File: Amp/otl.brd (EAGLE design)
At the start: 154.9 x 68.6 mm, 59 parts, among them X1 MOUNT-PAD2.0, X10 MOUNT-PAD2.0, X11 MOUNT-PAD2.0, X2 MOUNT-PAD2.0, X3 MOUNT-PAD2.0, X4 MOUNT-PAD2.0, X5 MOUNT-PAD2.0, X6 MOUNT-PAD2.0, X7 MOUNT-PAD2.0, X8 MOUNT-PAD2.0, X9 MOUNT-PAD2.0

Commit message: Made direct coupled
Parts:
- removed C13: 0.47uF, capacitor-wima:C22.5B11
- removed C14: 220uF/400V, my-cap:CPOL-RADIAL-25/12.5
- removed R25: 1.2k, my-res:AXIAL-0.8
- removed R26: 330, my-res:AXIAL-0.4
- removed R27: 1Meg, my-res:AXIAL-0.4
- removed R28: 100k, my-res:AXIAL-0.4
- added SJ1, SJ2: (no value), my-conn:SJ_2S-NO-LARGE
- added U1, U2: TLV431PTH, my-reg:TO-92
- C11: device capacitor-wima:C5B5.5 -> capacitor-wima:C22.5B11
- C12: value 1000uF/63V -> 220uF/400V; device my-cap:CPOL-RADIAL-16/7.5 -> my-cap:CPOL-RADIAL-25/12.5
- C2: value 0.47uF -> 470uF/63V; device capacitor-wima:C22.5B11 -> my-cap:CPOL-RADIAL-16/7.5
- C3: value 1000uF/63V -> 0.47uF; device my-cap:CPOL-RADIAL-16/7.5 -> capacitor-wima:C5B5.5
- C4: value 0.47uF -> 1000uF/63V; device capacitor-wima:C5B5.5 -> my-cap:CPOL-RADIAL-16/7.5
- C5: value 1000uF/63V -> 0.47uF; device my-cap:CPOL-RADIAL-16/7.5 -> capacitor-wima:C22.5B11
- C6: value 0.47uF -> 220uF/400V; device capacitor-wima:C22.5B11 -> my-cap:CPOL-RADIAL-25/12.5
- C7: value 220uF/400V -> 0.47uF; device my-cap:CPOL-RADIAL-25/12.5 -> capacitor-wima:C5B5.5
- C8: value 0.47uF -> 470uF/63V; device capacitor-wima:C5B5.5 -> my-cap:CPOL-RADIAL-16/7.5
- C9: device capacitor-wima:C22.5B11 -> capacitor-wima:C5B5.5
- R10, R22: value 750 -> 330; device my-res:AXIAL-0.8 -> my-res:AXIAL-0.4
- R11, R23: value 1.2k -> 1Meg; device my-res:AXIAL-0.8 -> my-res:AXIAL-0.4
- R12: value 330 -> 100k
- R14: value 100k -> 330
- R15: value 1Meg -> 68k; device my-res:AXIAL-0.4 -> my-res:AXIAL-0.8
- R16: value 330 -> 2k; device my-res:AXIAL-0.4 -> SparkFun-Electromechanical:3362U-2
- R17: value 240k -> 330
- R18: value 5.6k -> 750; device my-res:AXIAL-0.4 -> my-res:AXIAL-0.8
- R19: value 3Meg -> 1.5k; device my-res:AXIAL-0.4 -> my-res:AXIAL-0.8
- R20, R6: value 2.2Meg -> 750; device SparkFun-Electromechanical:3362U-2 -> my-res:AXIAL-0.8
- R21, R7: value 330 -> 1.5k; device my-res:AXIAL-0.4 -> my-res:AXIAL-0.8
- R24: value 750 -> 100k; device my-res:AXIAL-0.8 -> my-res:AXIAL-0.4
- R3: value 240k -> 68k; device my-res:AXIAL-0.4 -> my-res:AXIAL-0.8
- R4: value 5.6k -> 2k; device my-res:AXIAL-0.4 -> SparkFun-Electromechanical:3362U-2
- R5: value 3Meg -> 330
- R9: value 1.2k -> 1.5k
- moved X9 130.8 mm to (20.3, 34.3)
- moved X7 123.4 mm to (26.7, 22.9)
- moved R14 106.7 mm to (119.4, 47.0), turned to 0 degrees
- moved X3 105.6 mm to (132.1, 52.1)
- moved X11 102.9 mm to (26.7, 40.6)
- moved C7 101.2 mm to (109.2, 49.5), turned to 90 degrees
- moved X5 91.1 mm to (110.5, 63.5)
- moved X6 91.1 mm to (110.5, 5.08)
- moved C10 86.4 mm to (39.4, 43.2)
- moved R24 84.8 mm to (14.0, 38.1), turned to 180 degrees
- moved R19 74.9 mm to (39.4, 62.2), turned to 0 degrees
- moved C3 73.7 mm to (52.1, 22.9), turned to 0 degrees
- moved R13 59.4 mm to (119.4, 52.1), turned to 0 degrees
- moved C6 58.0 mm to (14.0, 15.2), turned to 0 degrees
- moved R17 53.9 mm to (74.9, 52.1)
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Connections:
- removed net N$22: C9.2, R20.2, R21.P$1
- removed net N$7: R5.P$1, R6.3
- net GND: now also C2.2, C7.2, C9.2, R12.P$1, R16.1, R19.P$1, R21.P$1, R24.P$1, R4.1, R7.P$1, SJ1.1, SJ2.1, U1.2, U2.2, X10.P$1, X11.P$1, X7.P$1, X8.P$1, X9.P$1; no longer C11.2, C12.2, C5.2, R14.P$1, R15.P$1, R18.P$1, R20.1, R25.P$1, R27.P$1, R28.P$1, R4.P$1, R6.1, X2.P$1, X3.P$1, X4.P$1, X5.P$1, X6.P$1
- net HT_L: now also R6.P$2, X6.P$1; no longer R10.P$2, R5.P$2, X11.P$1
- net HT_R: now also R15.P$2, R18.P$2, R20.P$2, X5.P$1; no longer R17.P$2, R19.P$2, R22.P$2, R24.P$2, X1.P$1
- net IN_L: now also X1.P$1; no longer X7.P$1
- net IN_R: now also R13.P$2, R14.P$1, X3.P$1; no longer R15.P$2, R16.P$1, X9.P$1
- net N$1: now also C5.1, R6.P$1; no longer C6.1, R10.P$1
- net N$10: now also R22.P$1; no longer R26.P$1
- net N$11: now also C6.1; no longer C7.1
- net N$12: now also C10.1, C9.1, R19.P$2, R21.P$2; no longer C11.1, C12.1, R23.P$2, R25.P$2
- net N$13: now also C11.2, R22.P$2, R23.P$2; no longer C13.2, R26.P$2, R27.P$2
- net N$14: now also R17.P$2; no longer R21.P$2
- net N$15: now also R16.2, SJ2.2, U2.1; no longer R19.P$1, R20.3
- net N$16: now also C7.1, R16.3, U2.3; no longer C10.1, R18.P$2
- net N$17: now also R15.P$1; no longer C9.1
- net N$18: now also C12.1; no longer C14.1
- net N$2: now also C11.1, R18.P$1, R20.P$1; no longer C13.1, R22.P$1, R24.P$1
- net N$20: now also R4.2, SJ1.2, U1.1; no longer C2.2, R6.2, R7.P$1
- net N$21: now also R14.P$2; no longer R16.P$2
- net N$3: now also R10.P$1; no longer R12.P$1
- net N$4: now also C2.1, R4.3, U1.3; no longer C3.1, R4.P$2
- net N$5: now also C3.1, R7.P$2; no longer C5.1, R11.P$2
- net N$6: now also C5.2, R10.P$2, R11.P$2; no longer C6.2, R12.P$2, R13.P$2
- net N$8: now also R5.P$2; no longer R7.P$2
- net N$9: now also R5.P$1; no longer C2.1
- net OUT_L: now also C6.2, R12.P$2, X2.P$1; no longer C7.2, R14.P$2, X8.P$1
- net OUT_R: now also C12.2, R24.P$2, X4.P$1; no longer C14.2, R28.P$2, X10.P$1
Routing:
- net N$22: track 44.7 -> 0.00 mm
- net N$4: track 39.8 -> 73.3 mm, vias 0 -> 3
- net N$20: track 44.7 -> 16.6 mm
- net N$16: track 36.8 -> 62.6 mm, vias 0 -> 3
- net N$21: track 21.2 -> 13.3 mm
- net N$15: track 7.71 -> 15.5 mm
- net N$7: track 7.73 -> 0.00 mm
- net N$17: track 61.8 -> 56.3 mm
- net N$19: track 11.0 -> 7.62 mm
- net N$9: track 58.9 -> 56.3 mm
- net HT_L: track 31.4 -> 29.3 mm
- net HT_R: track 31.4 -> 29.3 mm
- net IN_R: track 18.1 -> 19.9 mm
- net IN_L: track 18.1 -> 19.9 mm
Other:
- board size 154.9 x 68.6 mm -> 137.2 x 68.6 mm
- board text added: "GND"
- board text removed: "Vp"
- board text removed: "Vp/2"

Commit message: Tubes' names added
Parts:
- V1: value (none) -> 6SN7-GTB
- V2, V3: value (none) -> 6AS7-G
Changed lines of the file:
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@@
 <attribute name="VALUE" x="33.401" y="12.319" size="0.8128" layer="27" font="vector" ratio="20"/>
 </element>
-<element name="V1" library="my-tubes" package="OKTAL-OUTLET" value="" x="132.08" y="34.29" smashed="yes" rot="R90">
+<element name="V1" library="my-tubes" package="OKTAL-OUTLET" value="6SN7-GTB" x="132.08" y="34.29" smashed="yes" rot="R90">
 <attribute name="NAME" x="129.54" y="33.655" size="0.8128" layer="25" font="vector" ratio="20" rot="R90"/>
 <attribute name="VALUE" x="138.43" y="31.75" size="0.8128" layer="27" font="vector" ratio="15" rot="R90"/>
 </element>
-<element name="V2" library="my-tubes" package="OKTAL-OUTLET" value="" x="67.31" y="5.08" smashed="yes" rot="R180">
+<element name="V2" library="my-tubes" package="OKTAL-OUTLET" value="6AS7-G" x="67.31" y="5.08" smashed="yes" rot="R180">
 <attribute name="NAME" x="67.945" y="2.54" size="0.8128" layer="25" font="vector" ratio="20" rot="R180"/>
 <attribute name="VALUE" x="69.85" y="11.43" size="0.8128" layer="27" font="vector" ratio="15" rot="R180"/>
 </element>
-<element name="V3" library="my-tubes" package="OKTAL-OUTLET" value="" x="67.31" y="63.5" smashed="yes" rot="R180">
+<element name="V3" library="my-tubes" package="OKTAL-OUTLET" value="6AS7-G" x="67.31" y="63.5" smashed="yes" rot="R180">
 <attribute name="NAME" x="67.945" y="67.31" size="0.8128" layer="25" font="vector" ratio="20" rot="R180"/>
 <attribute name="VALUE" x="69.85" y="69.85" size="0.8128" layer="27" font="vector" ratio="15" rot="R180"/>

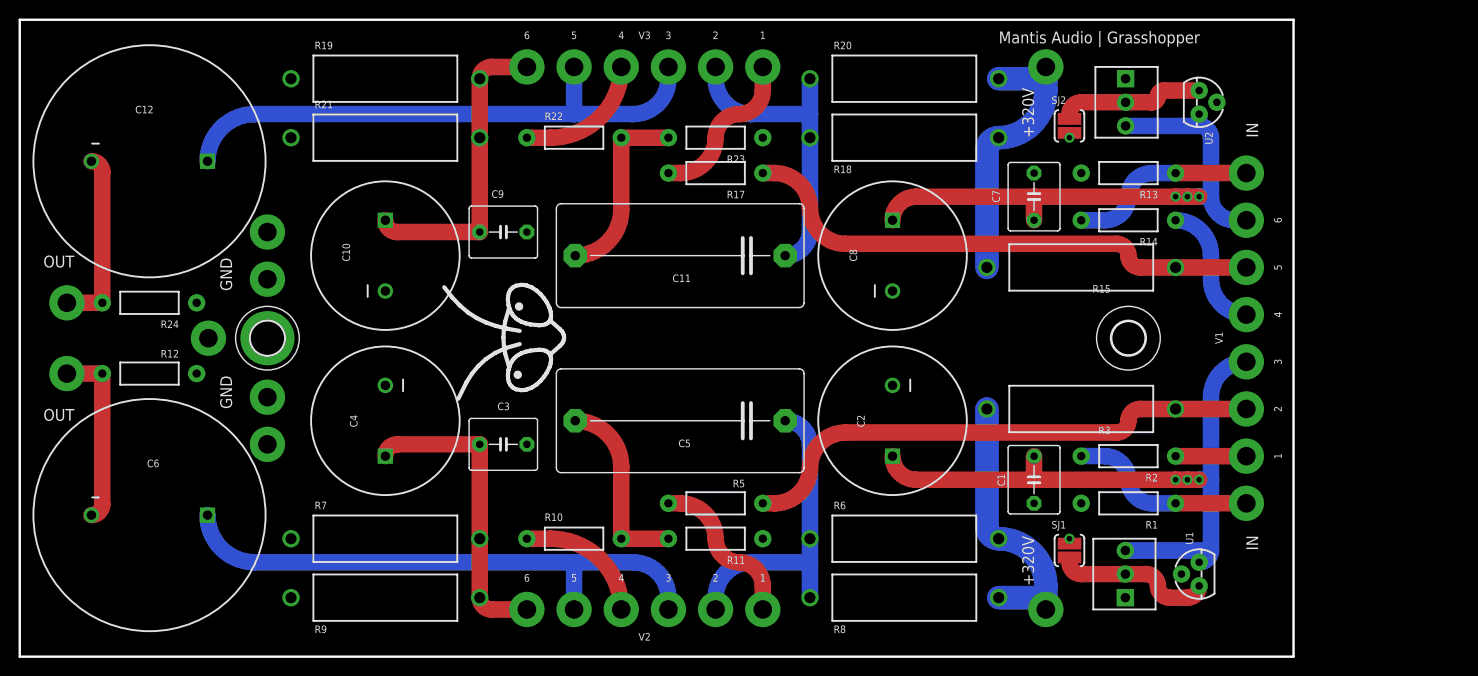
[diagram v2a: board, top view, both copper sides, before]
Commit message: More mounting holes
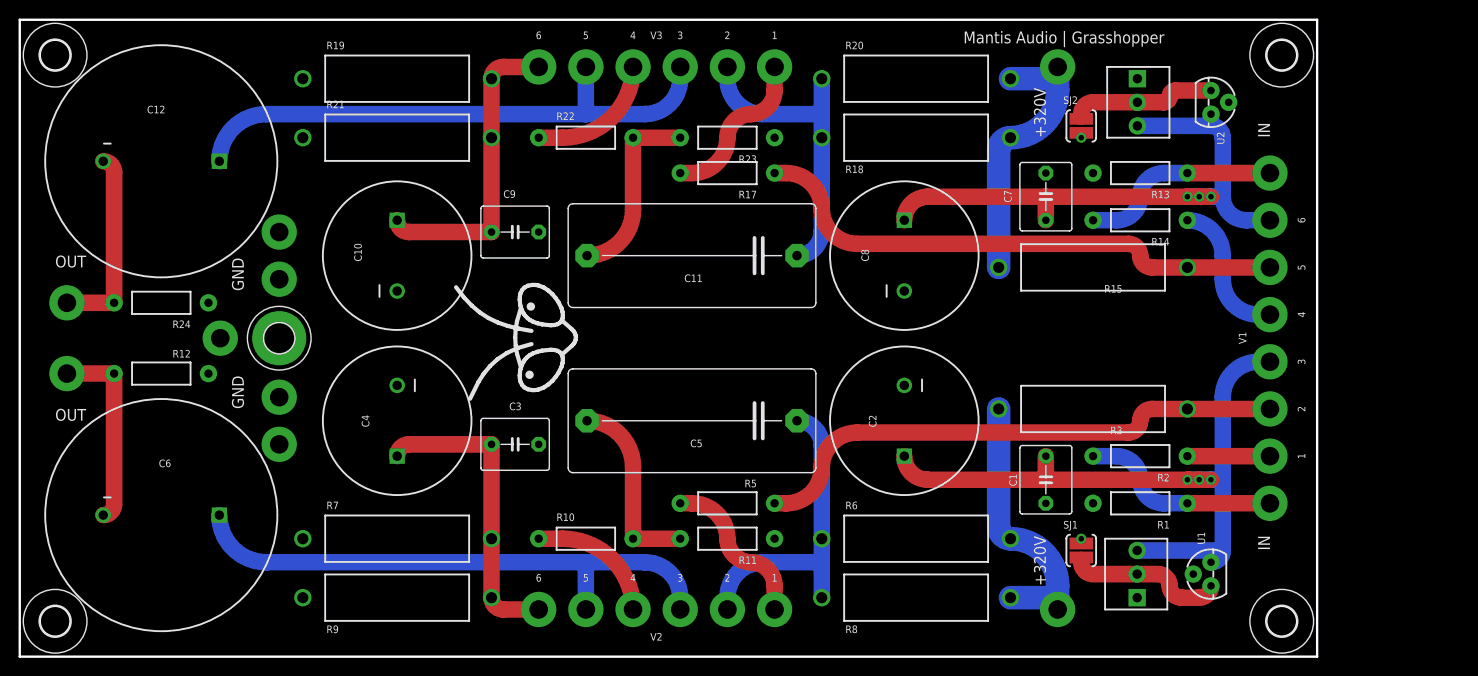
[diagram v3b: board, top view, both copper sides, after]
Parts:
- added H3, H4, H5: MOUNT-HOLE3.2, holes:3,2
- H1: value MOUNT-PAD-ROUND3.6 -> MOUNT-PAD-ROUND3.2; device holes:3,6-PAD -> holes:3,2-PAD
- H2: value MOUNT-HOLE3.6 -> MOUNT-HOLE3.2; device holes:3,6 -> holes:3,2
- moved H2 34.7 mm to (135.9, 64.8)
- moved V1 2.54 mm to (134.6, 34.3)
- moved X1 2.54 mm to (134.6, 16.5)
- moved X3 2.54 mm to (134.6, 52.1)
- moved R1 1.27 mm to (120.7, 16.5)
- moved R13 1.27 mm to (120.7, 52.1)
- moved R14 1.27 mm to (120.7, 47.0)
- moved R16 1.27 mm to (120.7, 59.7)
- moved R2 1.27 mm to (120.7, 21.6)
- moved U1 1.27 mm to (128.3, 8.89)
- moved U2 1.27 mm to (128.3, 59.7)
- moved X5 1.27 mm to (111.8, 63.5)
- moved X6 1.27 mm to (111.8, 5.08)
- moved C10 1.27 mm to (40.6, 43.2)
- moved C3 1.27 mm to (53.3, 22.9)
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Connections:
- net GND: now also H1.B3,2; no longer H1.B3,6
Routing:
- net OUT_L: track 19.5 -> 20.8 mm
- net N$9: track 56.3 -> 57.5 mm
- net N$17: track 56.3 -> 57.5 mm
- net IN_R: track 19.9 -> 21.2 mm
- net IN_L: track 19.9 -> 21.2 mm
- net OUT_R: track 19.5 -> 20.8 mm
- net N$21: track 13.3 -> 14.6 mm
- net N$19: track 7.62 -> 8.89 mm
- net N$16: track 62.6 -> 63.9 mm
- net N$4: track 73.3 -> 74.6 mm
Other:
- board size 137.2 x 68.6 mm -> 139.7 x 68.6 mm

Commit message: Small fix
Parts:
- R12, R24: value 100k -> 2.7k
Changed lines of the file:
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@@
 <attribute name="VALUE" x="78.486" y="13.081" size="0.8128" layer="27" font="vector" ratio="20" rot="R180"/>
 </element>
-<element name="R12" library="my-res" package="AXIAL-0.4" value="100k" x="15.24" y="30.48" smashed="yes" rot="R180">
+<element name="R12" library="my-res" package="AXIAL-0.4" value="2.7k" x="15.24" y="30.48" smashed="yes" rot="R180">
 <attribute name="NAME" x="18.415" y="33.02" size="0.8128" layer="25" font="vector" ratio="20" rot="R180"/>
 <attribute name="VALUE" x="17.526" y="30.861" size="0.8128" layer="27" font="vector" ratio="20" rot="R180"/>
@@
 <attribute name="VALUE" x="78.486" y="56.261" size="0.8128" layer="27" font="vector" ratio="20" rot="R180"/>
 </element>
-<element name="R24" library="my-res" package="AXIAL-0.4" value="100k" x="15.24" y="38.1" smashed="yes" rot="R180">
+<element name="R24" library="my-res" package="AXIAL-0.4" value="2.7k" x="15.24" y="38.1" smashed="yes" rot="R180">
 <attribute name="NAME" x="18.415" y="36.195" size="0.8128" layer="25" font="vector" ratio="20" rot="R180"/>
 <attribute name="VALUE" x="17.526" y="38.481" size="0.8128" layer="27" font="vector" ratio="20" rot="R180"/>
